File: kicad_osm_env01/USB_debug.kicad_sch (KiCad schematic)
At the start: 38 parts, among them J36 USB_C_Receptacle_USB2.0, U13 CP2102N-A02-GQFN24, U15 M74VHC1GT14DFT2G, U5 SP3003-02JTG

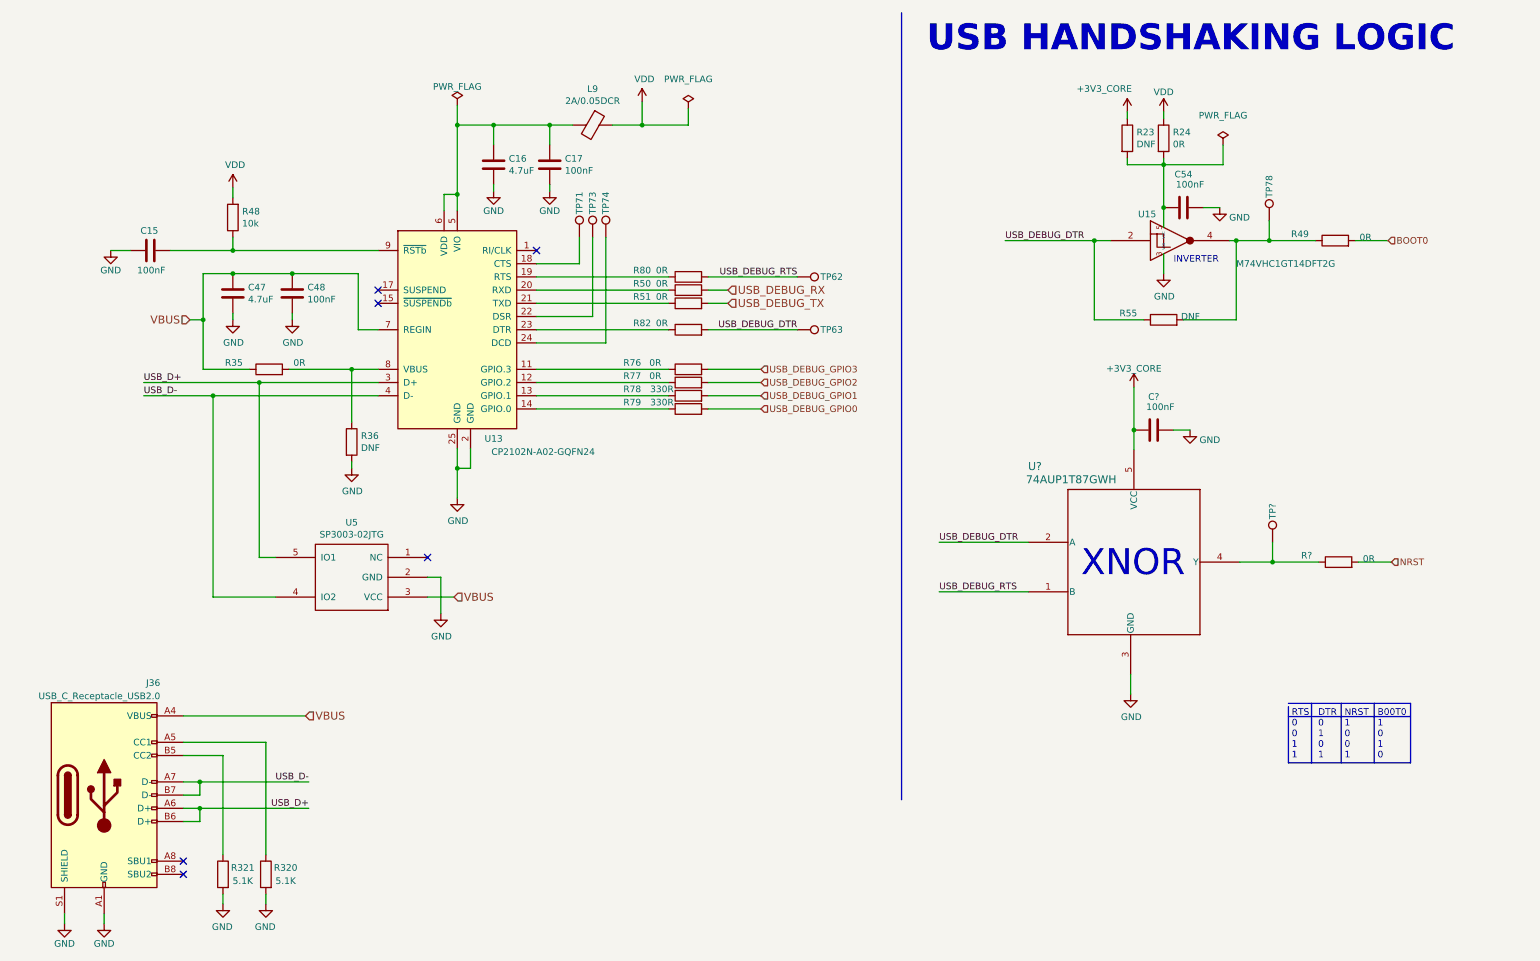
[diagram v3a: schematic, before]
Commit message: removed battery circuit and add usb c to schematics
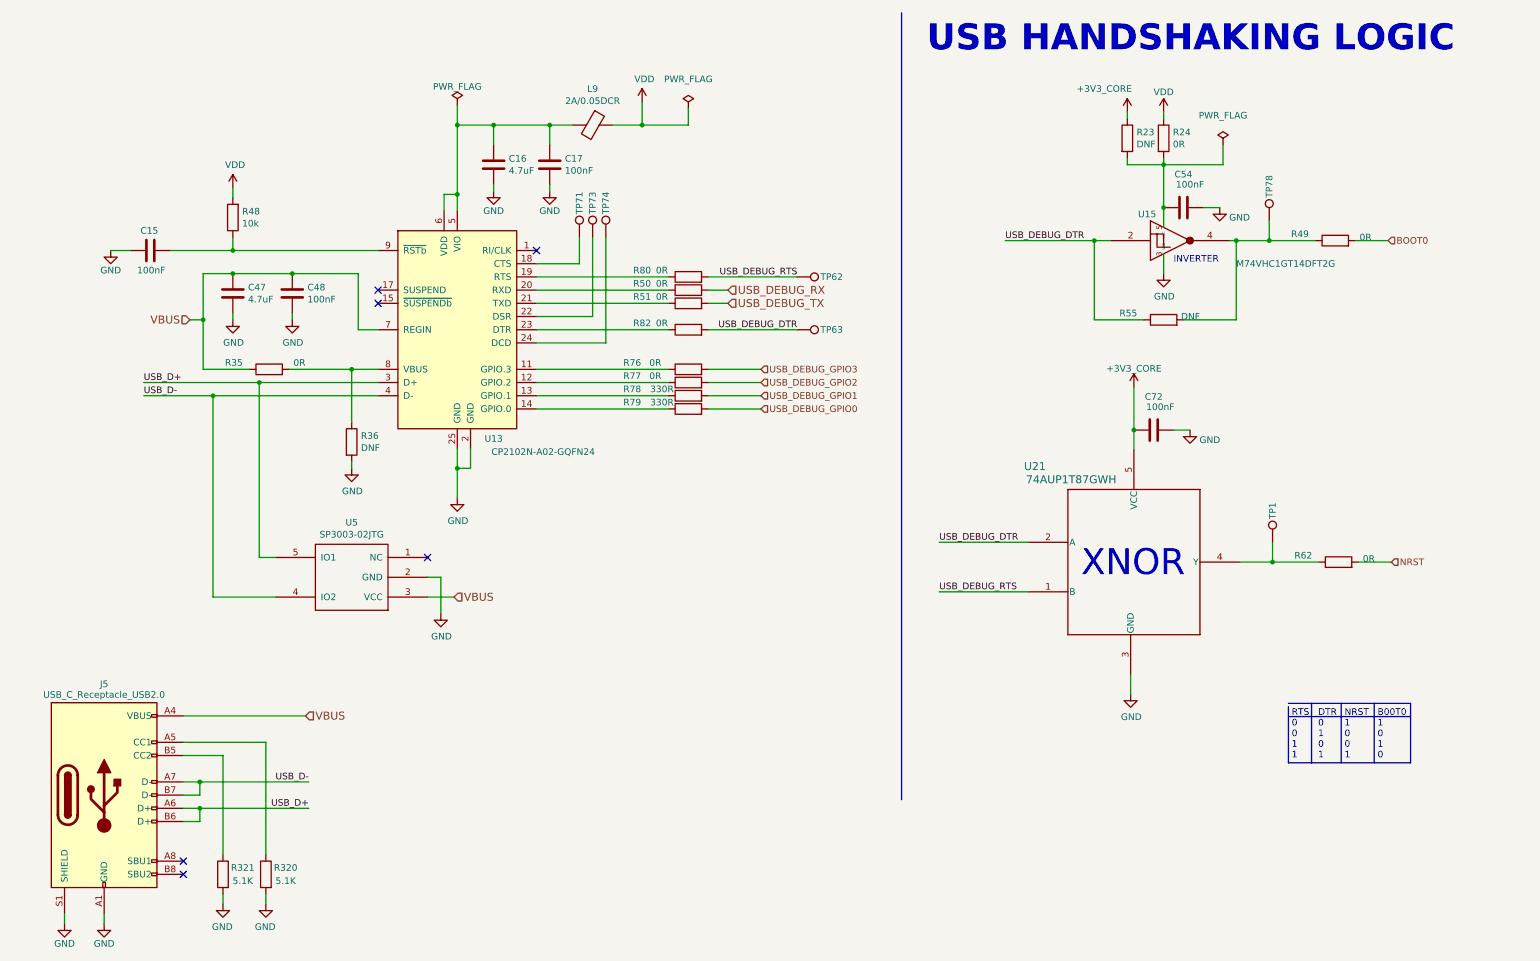
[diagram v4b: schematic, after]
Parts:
- removed J36: USB_C_Receptacle_USB2.0, Devtank_PCB_Lib:216989-0001_MOL, symbol Connector:USB_C_Receptacle_USB2.0
- added J5: USB_C_Receptacle_USB2.0, Footprints:MOLEX_216989-0001, symbol Symbols:USB_C_Receptacle_USB2.0
- gave numbers to parts that had none: 4
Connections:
- net GND: now also J5.A1 (GND), J5.A12 (GND), J5.B1 (GND), J5.B12 (GND), J5.S1 (SHIELD), J5.S2 (SHIELD), J5.S3 (SHIELD), J5.S4 (SHIELD)
- net USB_D+: now also J5.A6 (D+), J5.B6 (D+)
- net USB_D-: now also J5.A7 (D-), J5.B7 (D-)
- net VBUS: now also J5.A4 (VBUS), J5.A9 (VBUS), J5.B4 (VBUS), J5.B9 (VBUS)
- net at R320.1: now also J5.A5 (CC1)
- net at R321.1: now also J5.B5 (CC2)
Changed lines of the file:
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@@
   (symbol (lib_id "Device:R") (at 265.43 119.634 90) (unit 1)
     (in_bom yes) (on_board yes) (dnp no)
-    (property "Reference" "R?" (at 260.35 118.364 90)
+    (property "Reference" "R62" (at 260.35 118.364 90)
       (effects (font (size 1.27 1.27)) (justify left))
     )
@@
       (project "OSM_env01"
         (path "/ab8b0540-9c9f-4195-88f5-7bed0b0a8ed6/00000000-0000-0000-0000-00005f4610be"
-          (reference "R?") (unit 1)
+          (reference "R62") (unit 1)
         )
       )
@@
   (symbol (lib_id "Connector:TestPoint") (at 252.73 115.824 0) (unit 1)
     (in_bom yes) (on_board yes) (dnp no)
-    (property "Reference" "TP?" (at 252.73 111.379 90)
+    (property "Reference" "TP1" (at 252.73 111.379 90)
       (effects (font (size 1.27 1.27)) (justify left))
     )
@@
       (project "OSM_env01"
         (path "/ab8b0540-9c9f-4195-88f5-7bed0b0a8ed6/00000000-0000-0000-0000-00005f4610be"
-          (reference "TP?") (unit 1)
+          (reference "TP1") (unit 1)
         )
       )
@@
   (symbol (lib_id "Device:C") (at 229.87 94.234 270) (unit 1)
     (in_bom yes) (on_board yes) (dnp no)
-    (property "Reference" "C?" (at 229.87 87.8332 90)
+    (property "Reference" "C72" (at 229.87 87.8332 90)
       (effects (font (size 1.27 1.27)))
     )
@@
       (project "OSM_env01"
         (path "/ab8b0540-9c9f-4195-88f5-7bed0b0a8ed6/00000000-0000-0000-0000-00005f4610be"
-          (reference "C?") (unit 1)
+          (reference "C72") (unit 1)
         )
       )
@@
   (symbol (lib_id "power:GND") (at 236.855 94.234 0) (unit 1)
     (in_bom yes) (on_board yes) (dnp no)
-    (property "Reference" "#PWR?" (at 236.855 100.584 0)
+    (property "Reference" "#PWR0113" (at 236.855 100.584 0)
       (effects (font (size 1.27 1.27)) hide)
     )
@@
       (project "OSM_env01"
         (path "/ab8b0540-9c9f-4195-88f5-7bed0b0a8ed6/00000000-0000-0000-0000-00005f4610be"
-          (reference "#PWR?") (unit 1)
+          (reference "#PWR0113") (unit 1)
         )
       )
@@
   (symbol (lib_id "power:GND") (at 225.425 145.034 0) (unit 1)
     (in_bom yes) (on_board yes) (dnp no)
-    (property "Reference" "#PWR?" (at 225.425 151.384 0)
+    (property "Reference" "#PWR0135" (at 225.425 151.384 0)
       (effects (font (size 1.27 1.27)) hide)
     )
@@
       (project "OSM_env01"
         (path "/ab8b0540-9c9f-4195-88f5-7bed0b0a8ed6/00000000-0000-0000-0000-00005f4610be"
-          (reference "#PWR?") (unit 1)
+          (reference "#PWR0135") (unit 1)
         )
       )
@@
     )
   )
-  (symbol (lib_id "Connector:TestPoint") (at 121.92 57.15 0) (unit 1)
-    (in_bom yes) (on_board yes) (dnp no)
-    (property "Reference" "TP73" (at 121.92 52.705 90)
-      (effects (font (size 1.27 1.27)) (justify left))
-    )
-    (property "Value" "Test_Point" (at 123.3932 56.4642 0)
-      (effects (font (size 1.27 1.27)) (justify left) hide)
-    )
-    (property "Footprint" "TestPoint:TestPoint_THTPad_D1.0mm_Drill0.5mm" (at 127 57.15 0)
-      (effects (font (size 1.27 1.27)) hide)
-    )
-    (property "Datasheet" "~" (at 127 57.15 0)
-      (effects (font (size 1.27 1.27)) hide)
-    )
-    (pin "1")
-    (instances
-      (project "OSM_env01"
-        (path "/ab8b0540-9c9f-4195-88f5-7bed0b0a8ed6/00000000-0000-0000-0000-00005f4610be"
-          (reference "TP73") (unit 1)
-        )
-      )
-    )
-  )
-  (symbol (lib_id "power:GND") (at 50.8 185.42 0) (mirror y) (unit 1)
-    (in_bom yes) (on_board yes) (dnp no)
-    (property "Reference" "#PWR0143" (at 50.8 191.77 0)
-      (effects (font (size 1.27 1.27)) hide)
-    )
-    (property "Value" "GND" (at 50.673 189.8142 0)
-      (effects (font (size 1.27 1.27)))
-    )
-    (property "Footprint" "" (at 50.8 185.42 0)
-      (effects (font (size 1.27 1.27)) hide)
-    )
-    (property "Datasheet" "" (at 50.8 185.42 0)
-      (effects (font (size 1.27 1.27)) hide)
-    )
-    (pin "1")
-    (instances
-      (project "CM4IOv5"
-        (path "/0ce072f6-fe22-4a72-b3d5-0701aeebf00d/00000000-0000-0000-0000-00005e072e02"
-          (reference "#PWR0143") (unit 1)
-        )
-      )
-      (project "HILTOP_Motherboard"
-        (path "/657f798a-f366-463e-bf09-ea2fb410f19a"
-          (reference "#PWR0466") (unit 1)
-        )
-      )
-      (project "OSM_env01"
-        (path "/ab8b0540-9c9f-4195-88f5-7bed0b0a8ed6/00000000-0000-0000-0000-00005f4610be"
-          (reference "#PWR093") (unit 1)
-        )
-      )
-    )
-  )
-  (symbol (lib_id "Connector:USB_C_Receptacle_USB2.0") (at 27.94 164.465 0) (unit 1)
-    (in_bom yes) (on_board yes) (dnp no)
-    (property "Reference" "J36" (at 38.735 142.875 0)
-      (effects (font (size 1.27 1.27)) (justify right))
-    )
-    (property "Value" "USB_C_Receptacle_USB2.0" (at 38.735 145.415 0)
-      (effects (font (size 1.27 1.27)) (justify right))
-    )
-    (property "Footprint" "Devtank_PCB_Lib:216989-0001_MOL" (at 31.75 164.465 0)
+  (symbol (lib_id "Symbols:USB_C_Receptacle_USB2.0") (at 27.94 164.465 0) (unit 1)
+    (in_bom yes) (on_board yes) (dnp no) (fields_autoplaced)
+    (property "Reference" "J5" (at 27.94 143.105 0)
+      (effects (font (size 1.27 1.27)))
+    )
+    (property "Value" "USB_C_Receptacle_USB2.0" (at 27.94 145.153 0)
+      (effects (font (size 1.27 1.27)))
+    )
+    (property "Footprint" "Footprints:MOLEX_216989-0001" (at 31.75 164.465 0)
       (effects (font (size 1.27 1.27)) hide)
     )
@@
     (pin "B9")
     (pin "S1")
-    (instances
+    (pin "S2")
+    (pin "S3")
+    (pin "S4")
+    (instances
+      (project "OSM_env01"
+        (path "/ab8b0540-9c9f-4195-88f5-7bed0b0a8ed6/00000000-0000-0000-0000-00005f4610be"
+          (reference "J5") (unit 1)
+        )
+      )
+    )
+  )
+  (symbol (lib_id "Connector:TestPoint") (at 121.92 57.15 0) (unit 1)
+    (in_bom yes) (on_board yes) (dnp no)
+    (property "Reference" "TP73" (at 121.92 52.705 90)
+      (effects (font (size 1.27 1.27)) (justify left))
+    )
+    (property "Value" "Test_Point" (at 123.3932 56.4642 0)
+      (effects (font (size 1.27 1.27)) (justify left) hide)
+    )
+    (property "Footprint" "TestPoint:TestPoint_THTPad_D1.0mm_Drill0.5mm" (at 127 57.15 0)
+      (effects (font (size 1.27 1.27)) hide)
+    )
+    (property "Datasheet" "~" (at 127 57.15 0)
+      (effects (font (size 1.27 1.27)) hide)
+    )
+    (pin "1")
+    (instances
+      (project "OSM_env01"
+        (path "/ab8b0540-9c9f-4195-88f5-7bed0b0a8ed6/00000000-0000-0000-0000-00005f4610be"
+          (reference "TP73") (unit 1)
+        )
+      )
+    )
+  )
+  (symbol (lib_id "power:GND") (at 50.8 185.42 0) (mirror y) (unit 1)
+    (in_bom yes) (on_board yes) (dnp no)
+    (property "Reference" "#PWR0143" (at 50.8 191.77 0)
+      (effects (font (size 1.27 1.27)) hide)
+    )
+    (property "Value" "GND" (at 50.673 189.8142 0)
+      (effects (font (size 1.27 1.27)))
+    )
+    (property "Footprint" "" (at 50.8 185.42 0)
+      (effects (font (size 1.27 1.27)) hide)
+    )
+    (property "Datasheet" "" (at 50.8 185.42 0)
+      (effects (font (size 1.27 1.27)) hide)
+    )
+    (pin "1")
+    (instances
+      (project "CM4IOv5"
+        (path "/0ce072f6-fe22-4a72-b3d5-0701aeebf00d/00000000-0000-0000-0000-00005e072e02"
+          (reference "#PWR0143") (unit 1)
+        )
+      )
       (project "HILTOP_Motherboard"
         (path "/657f798a-f366-463e-bf09-ea2fb410f19a"
-          (reference "J36") (unit 1)
-        )
-      )
-      (project "OSM_env01"
-        (path "/ab8b0540-9c9f-4195-88f5-7bed0b0a8ed6/00000000-0000-0000-0000-00005f4610be"
-          (reference "J5") (unit 1)
+          (reference "#PWR0466") (unit 1)
+        )
+      )
+      (project "OSM_env01"
+        (path "/ab8b0540-9c9f-4195-88f5-7bed0b0a8ed6/00000000-0000-0000-0000-00005f4610be"
+          (reference "#PWR093") (unit 1)
         )
       )
@@
   (symbol (lib_id "Devtank:+3V3_CORE") (at 226.06 85.979 0) (unit 1)
     (in_bom yes) (on_board yes) (dnp no) (fields_autoplaced)
-    (property "Reference" "#PWR?" (at 226.06 89.789 0)
+    (property "Reference" "#PWR0132" (at 226.06 89.789 0)
       (effects (font (size 1.27 1.27)) hide)
     )
@@
       (project "OSM_env01"
         (path "/ab8b0540-9c9f-4195-88f5-7bed0b0a8ed6/00000000-0000-0000-0000-00005f4610be"
-          (reference "#PWR?") (unit 1)
+          (reference "#PWR0132") (unit 1)
         )
       )
@@
   (symbol (lib_id "Devtank:74AUP1T87GWH") (at 205.74 110.744 0) (unit 1)
     (in_bom yes) (on_board yes) (dnp no)
-    (property "Reference" "U?" (at 207.01 101.219 0)
+    (property "Reference" "U21" (at 207.01 101.219 0)
       (effects (font (size 1.524 1.524)))
     )
@@
       (project "OSM_env01"
         (path "/ab8b0540-9c9f-4195-88f5-7bed0b0a8ed6/00000000-0000-0000-0000-00005f4610be"
-          (reference "U?") (unit 1)
-        )
-      )
+          (reference "U21") (unit 1)
+        )
+      )

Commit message: removed io module and 5V regulator
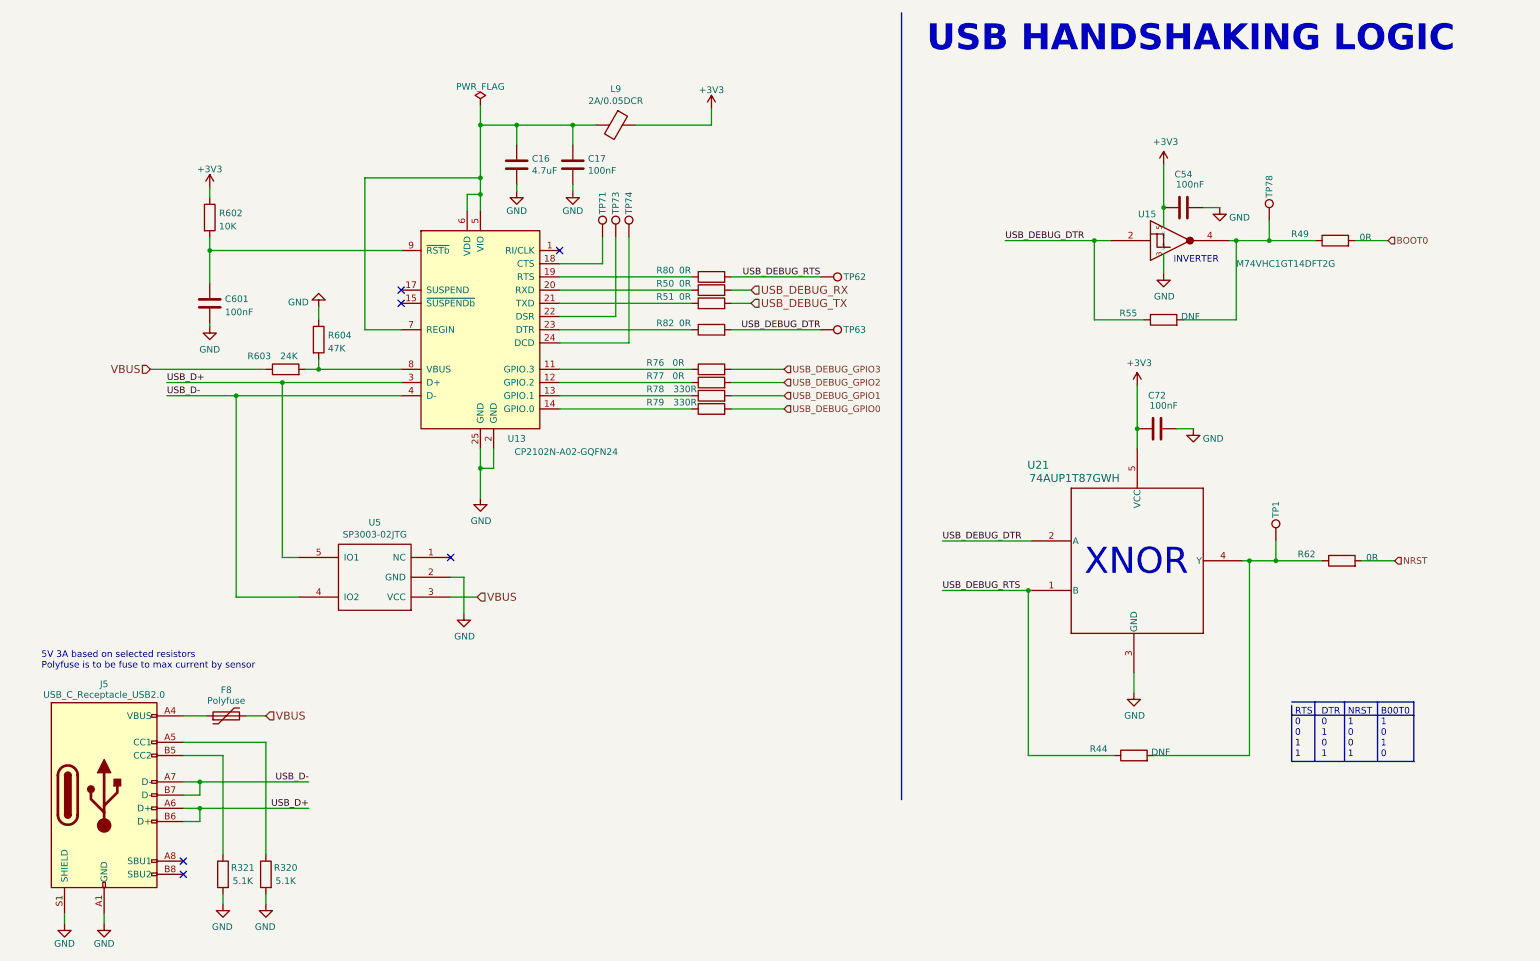
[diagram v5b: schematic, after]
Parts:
- removed C15, C48: 100nF, Capacitor_SMD:C_0402_1005Metric, symbol Device:C
- removed C47: 4.7uF, Capacitor_SMD:C_0402_1005Metric, symbol Device:C
- removed R23, R36: DNF, Resistor_SMD:R_0603_1608Metric, symbol Device:R
- removed R24, R35: 0R, Resistor_SMD:R_0603_1608Metric, symbol Device:R
- removed R48: 10k, Resistor_SMD:R_0603_1608Metric, symbol Device:R
- added C601: 100nF, Capacitor_SMD:C_0402_1005Metric, symbol Device:C
- added F8: Polyfuse, symbol Device:Polyfuse
- added R44: DNF, Resistor_SMD:R_0603_1608Metric, symbol Device:R
- added R602: 10K, Resistor_SMD:R_0603_1608Metric, symbol Device:R
- added R603: 24K, Resistor_SMD:R_0603_1608Metric, symbol Device:R
- added R604: 47K, Resistor_SMD:R_0603_1608Metric, symbol Device:R
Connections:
- net +3V3_CORE is gone; now on net +3V3: C72.2, U21.5 (VCC)
- net VDD is gone; now on net +3V3: L9.1
- net GND: now also C601.2, R604.1
- net USB_DEBUG_RTS: now also R44.1
- net VBUS: now also F8.2, R603.1; no longer J5.A4 (VBUS), J5.A9 (VBUS), J5.B4 (VBUS), J5.B9 (VBUS), U13.7 (REGIN)
- net at C16.1, C17.1, L9.2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: now also U13.7 (REGIN)
- net at U13.8 (VBUS): now also R603.2, R604.2
- net at U13.9 (~{RSTb}): now also C601.1, R602.2
- net +3V3: now reaches C54.2, U15.5 (VCC)
- net +3V3: now also R602.1
- net at R62.1, TP1.1, U21.4 (Y): now also R44.2
- new net: F8.1, J5.A4 (VBUS), J5.A9 (VBUS), J5.B4 (VBUS), J5.B9 (VBUS)
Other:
- note added: "5V 3A based on selected resistors Polyfuse is to be fuse to max current by sensor"
- moved on the sheet: C16, C17, C72, L9, R50, R51, R62, R76, R77, R78, R79, R80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
